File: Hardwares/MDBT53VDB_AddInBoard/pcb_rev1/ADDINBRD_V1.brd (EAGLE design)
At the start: 25 x 40 mm, 22 parts, among them CN1 51296-0894, CN2 IF_6PIN, CN3 IF_3PIN, CN4 IF_5PIN_H, CN5 IF_2PIN, Q1 BSS84AKQBZ, SW1 SKTADAE010, U1 RV-3028-C7

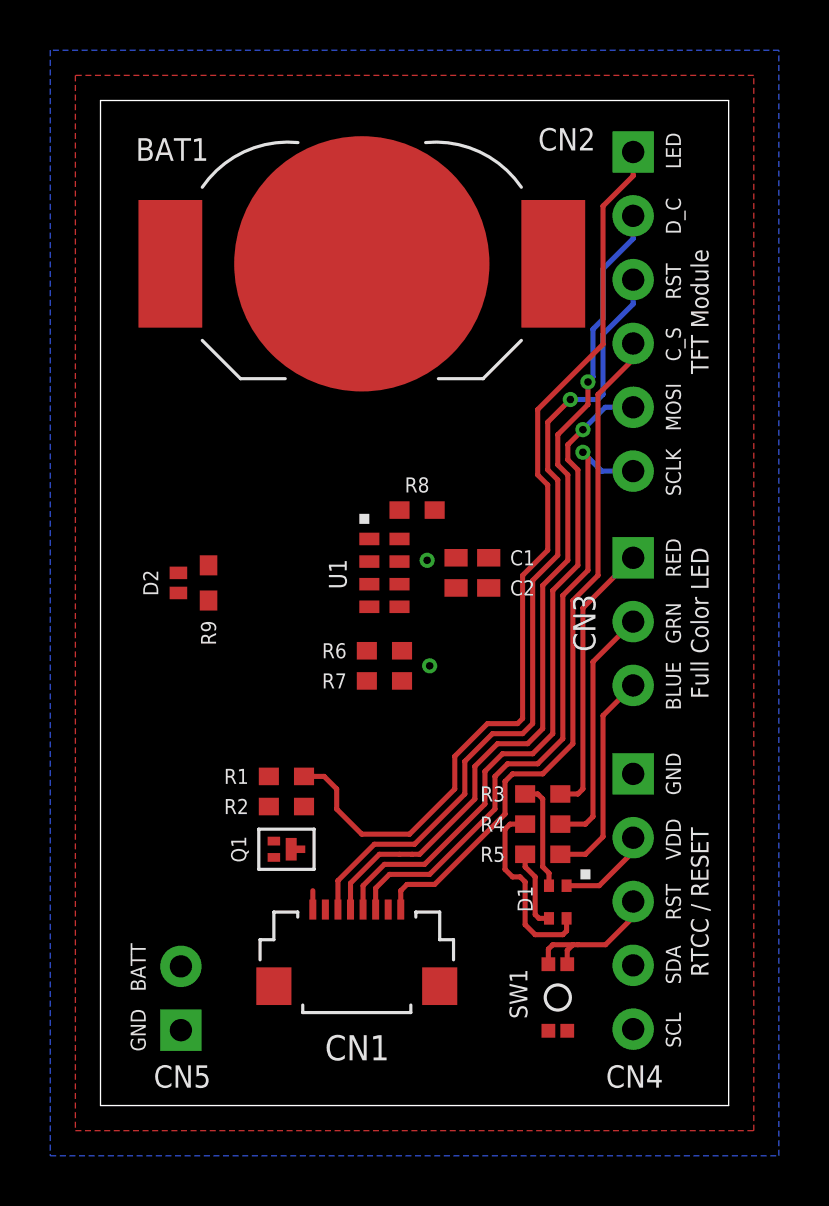
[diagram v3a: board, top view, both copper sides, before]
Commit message: レイアウトを修正
・一通りの配線を完了
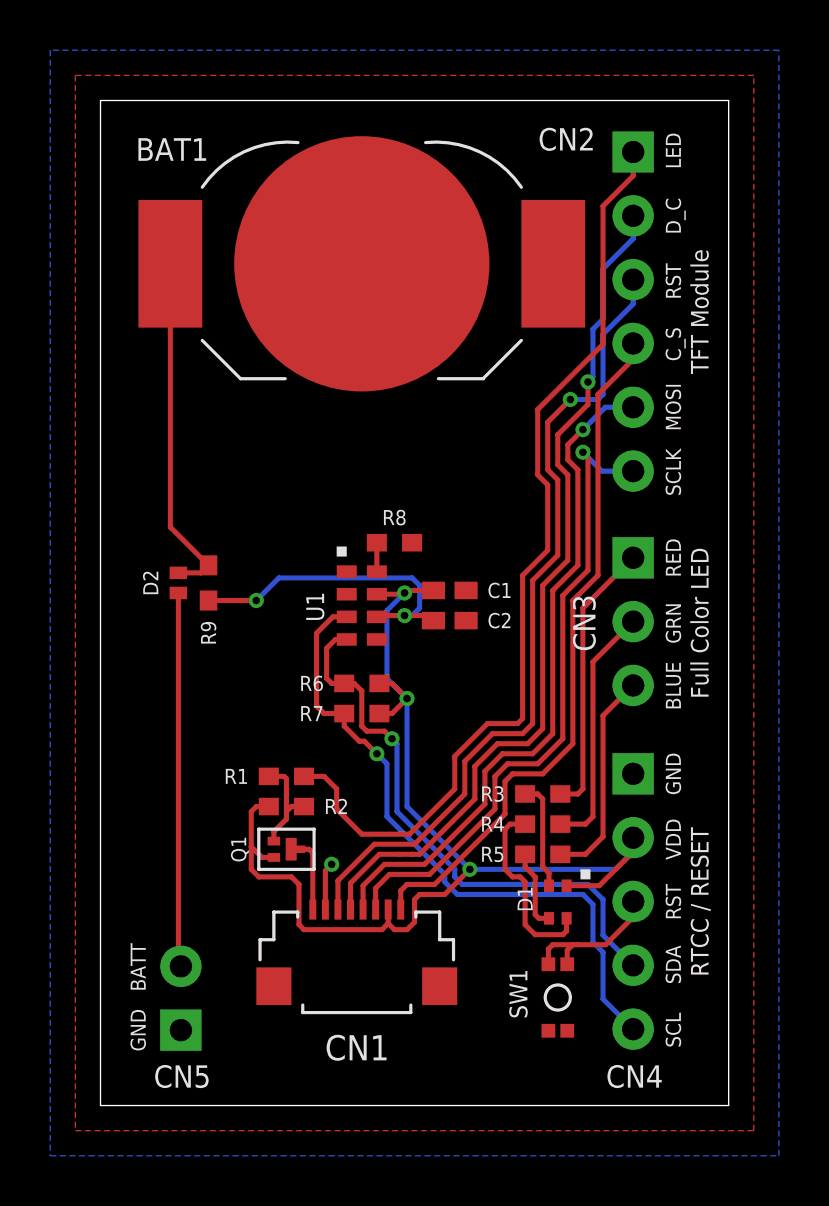
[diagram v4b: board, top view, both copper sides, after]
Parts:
- moved C1 1.58 mm to (13.9, 20.5)
- moved C2 1.58 mm to (13.9, 19.3)
- moved R6 1.58 mm to (10.4, 16.8)
- moved R8 1.58 mm to (11.7, 22.4)
- moved U1 1.58 mm to (9.40, 21.5)
- moved R7 1.58 mm to (10.4, 15.6)
- turned R2 to 180 degrees
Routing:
- net VDD: track 3.77 -> 46.4 mm, vias 2 -> 3
- net TWI_SCL: track 0.00 -> 26.0 mm, vias 0 -> 1
- net TWI_SDA: track 0.00 -> 22.5 mm, vias 0 -> 1
- net N$2: track 0.00 -> 14.9 mm
- net VDD_BATT: track 0.00 -> 14.0 mm
- net N$3: track 0.00 -> 12.9 mm, vias 0 -> 2
- net N$1: track 0.00 -> 4.21 mm
- net LEDA: track 0.75 -> 3.17 mm
- net 0V: track 0.00 -> 1.90 mm, vias 0 -> 1
- net N$4: track 0.00 -> 1.15 mm
